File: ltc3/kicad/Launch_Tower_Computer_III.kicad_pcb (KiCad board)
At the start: 2 copper layers, 250 x 135 mm, 356 parts, among them IC601 TLP3542, IC701 TLP3542, IC702 TLP3542, IC703 TLP3542, IC704 TLP3542, IC801 TLP3542, IC802 TLP3542, IC803 TLP3542, IC804 TLP3542, J601 RJ45, M801 W28-XQ1A-0.25, M802 W28-XQ1A-0.25, M803 W28-XQ1A-0.25, M804 W28-XQ1A-0.25, P201 PV_IN, P202 LAB_IN, P203 S2BPHKS, P301 CONN_BATT_MAIN, P303 CONN_BATT_SENSE, P305 S2BPHKS, P306 CONN_01X02, P402 CONN_01X04, P501 BeagleBone_Black_Expansion_He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, P502 BeagleBone_Black_Expansion_He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, P601 BATT-IN, P602 CONN_01x02, P603 UMBILICAL, P604 CONN_01x02, P605 CONN_01x02, P701 43045-1000, P703 43045-0800, P705 43045-0800, P801 43045-1000, P802 43025-1000, P803 CONN_EXT_PWR_1, P804 CONN_EXT_PWR_2, P805 43045-0800, P806 43025-0800, P807 CONN_EXT_PWR_3, P808 CONN_EXT_PWR_4, Q201 BSC028N06NS, Q202 BSC028N06NS, Q203 BSC028N06NS, Q204 BSC028N06NS, Q205 ZVN4525E6, Q206 Q_PMOS_DGS, Q207 Q_NPN_BCE, Q301 MMBT3904, Q302 SUM110P08-11, Q303 SUM110P08-11, Q304 SUM110P08-11, Q305 SUM110P08-11, Q306 NDS9407, Q601 PMV45EN, Q602 PMV45EN, Q701 PMV45EN, Q702 PMV45EN, Q703 PMV45EN, Q704 PMV45EN, Q801 PMV45EN, Q802 PMV45EN, Q803 PMV45EN, Q804 PMV45EN, SW401 SPST_switch, SW402 SP3T, SW403 SP3T, SW601 SPST_switch, SW801 SP3T, SW802 SP3T, SW803 SP3T, SW804 SP3T, U201 PI2127, U202 PI2127, U203 LTC2990, U204 LT8490, U301 LTC2990, U302 BQ77PL900, U401 PTN78020W, U402 LTC2991, U403 PTN78020H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

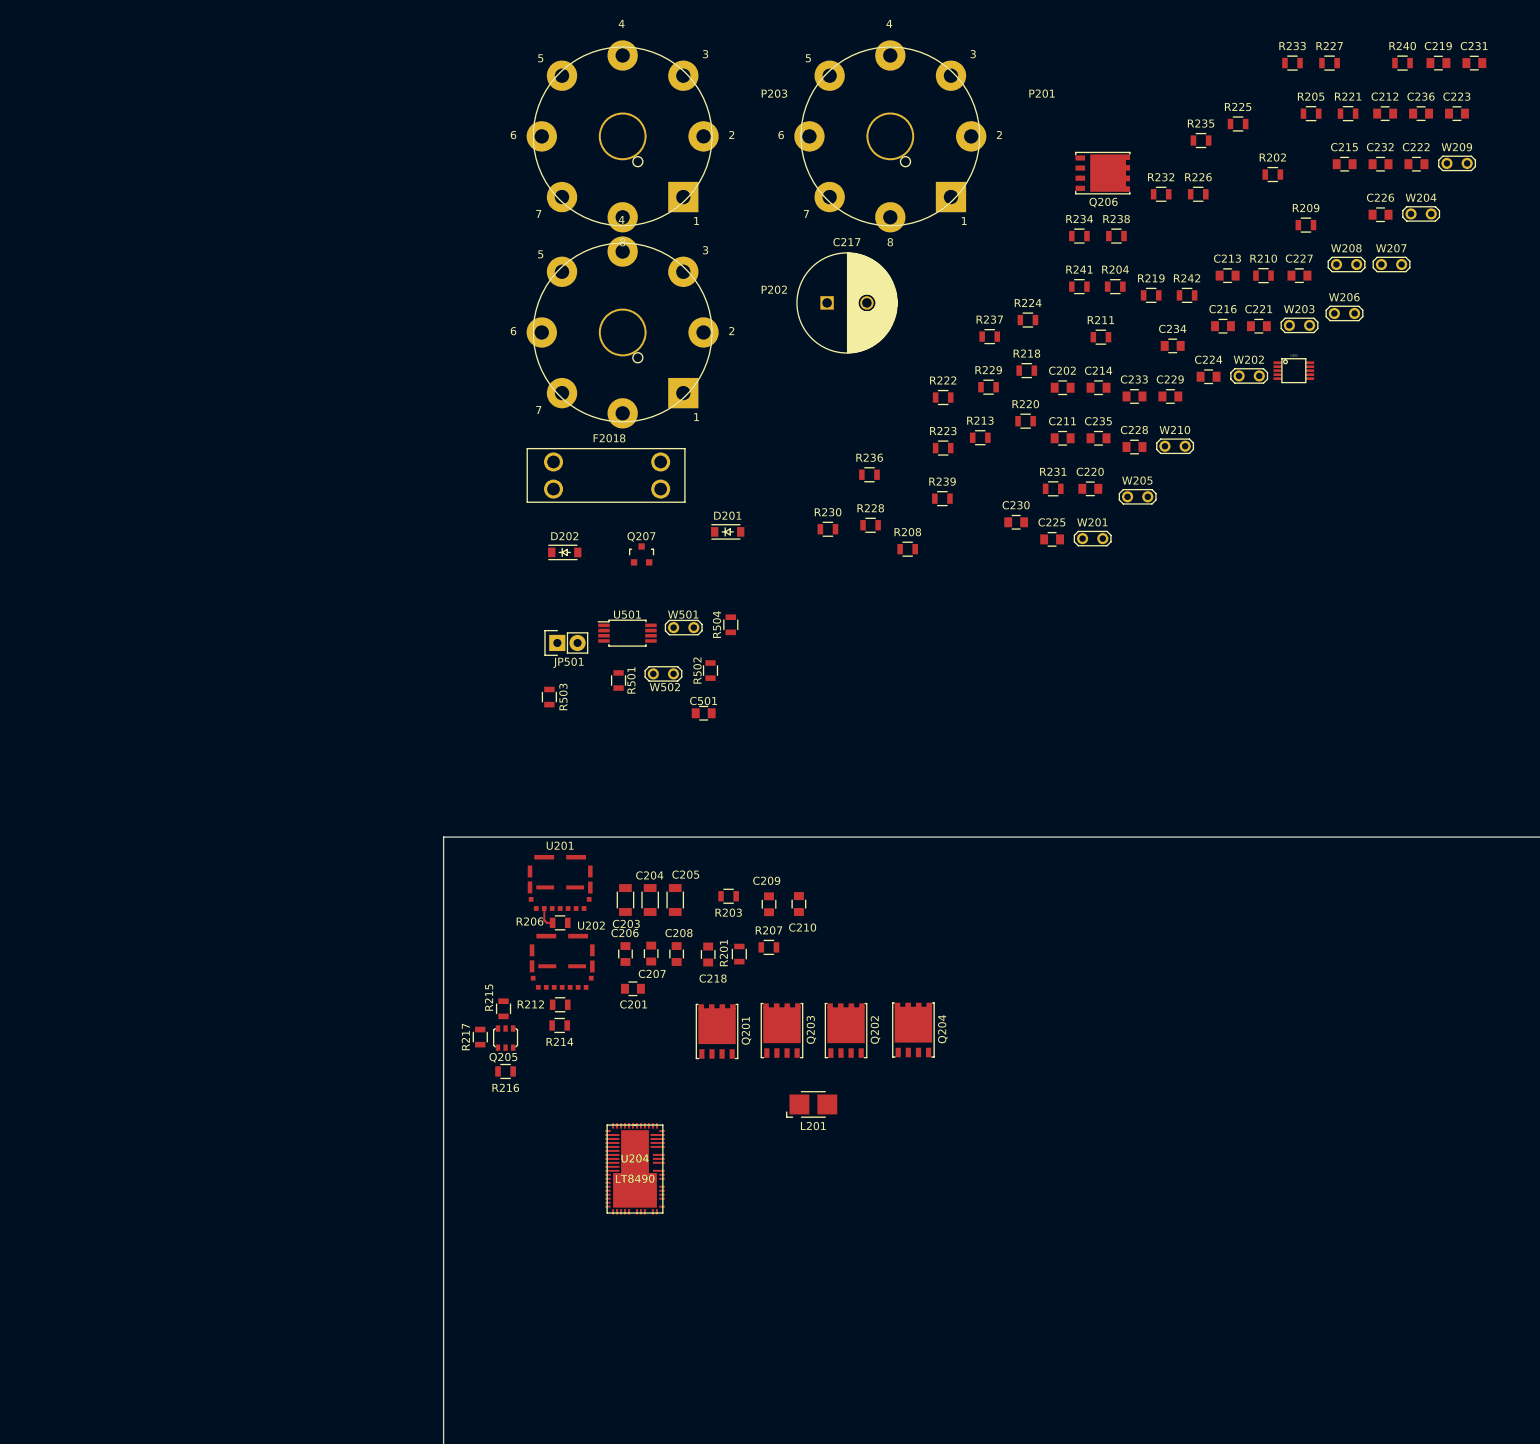
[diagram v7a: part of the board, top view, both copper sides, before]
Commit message: LTC3: Board Layout
Continued layout of power section of LTC3
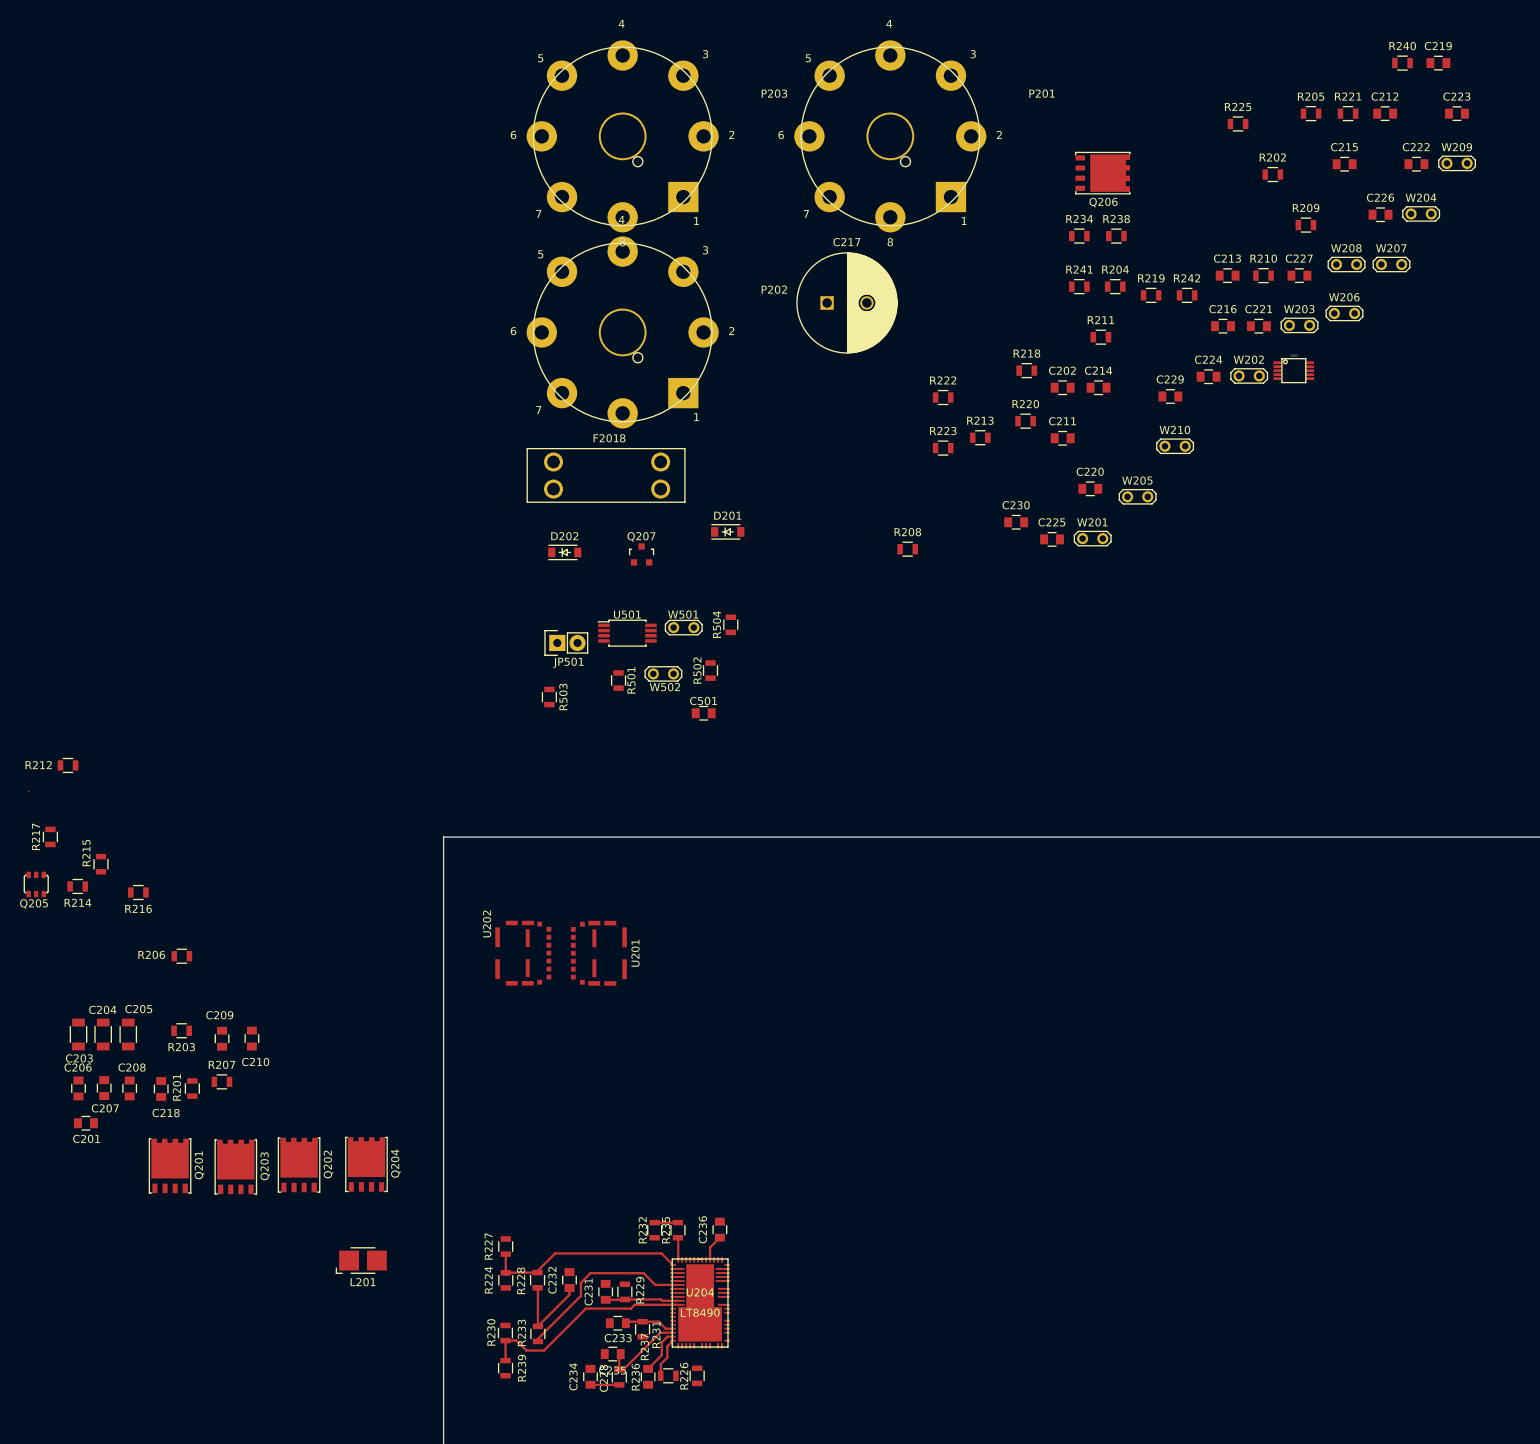
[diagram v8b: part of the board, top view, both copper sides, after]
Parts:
- moved C231 189.0 mm to (118.1, 119.4), turned to 90 degrees
- moved R233 187.7 mm to (105.5, 124.5), turned to 270 degrees
- moved R227 181.1 mm to (105.6, 113.7), turned to 90 degrees
- moved C232 173.3 mm to (113.6, 117.9), turned to 90 degrees
- moved C236 165.6 mm to (132.5, 111.6), turned to 90 degrees
- moved R226 161.2 mm to (129.6, 129.9), turned to 90 degrees
- moved R235 153.1 mm to (124.3, 111.6), turned to 270 degrees
- moved C234 148.7 mm to (116.2, 130.0), turned to 90 degrees
- moved R232 143.6 mm to (127.2, 111.6), turned to 90 degrees
- moved R224 137.3 mm to (105.6, 117.9), turned to 90 degrees
- moved R237 136.6 mm to (126.0, 129.9)
- moved C233 133.3 mm to (119.6, 123.3), turned to 180 degrees
- moved C228 131.8 mm to (123.4, 130.0), turned to 270 degrees
- moved C235 130.2 mm to (119.0, 127.2), turned to 180 degrees
- moved R229 122.5 mm to (120.5, 119.4), turned to 90 degrees
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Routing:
- net Net-(R233-Pad2): track 0.00 -> 27.0 mm
- net Net-(R224-Pad2): track 0.00 -> 25.1 mm
- net Net-(R230-Pad1): track 0.00 -> 22.9 mm
- net Net-(C232-Pad1): track 0.00 -> 11.3 mm
- net Net-(C235-Pad1): track 0.00 -> 10.7 mm
- net Net-(C233-Pad1): track 0.00 -> 9.31 mm
- net Net-(C231-Pad1): track 0.00 -> 9.11 mm
- net Net-(C228-Pad1): track 0.00 -> 5.75 mm
- net Net-(R237-Pad1): track 0.00 -> 5.05 mm
- net Net-(C234-Pad1): track 0.00 -> 3.63 mm
- net Net-(C236-Pad1): track 0.00 -> 3.30 mm
- net Net-(R232-Pad1): track 0.00 -> 2.79 mm
- net Net-(R206-Pad1): track 2.66 -> 0.00 mm
- added copper zone on F.Cu, net VBATT
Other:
- net class Default: clearance 1 -> 0.1; trace_width 7.19 -> 0.3
- rule trace_clearance: 1 -> 0.1
